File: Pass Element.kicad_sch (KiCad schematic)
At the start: 7 parts, among them Q601 BC846, Q602 MCU18P10Y-TP

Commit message: fix: bom improvements & more notes
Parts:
- D601: Notes (none) -> VZ = 10 V, suitable for input over-voltage clamping
- Q601: Notes (none) -> VCEO > 65 V for 50 V rail, IC small, used as gate pull-down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
- Q602: Notes (none) -> VDS > 100 V, ID > 2 A, P-channel device suitable for high-s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
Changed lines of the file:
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@@
+			)
+		)
+		(property "Notes" "VCEO > 65 V for 50 V rail, IC small, used as gate pull-down switch"
+			(at 149.86 105.41 0)
+			(effects
+				(font
+					(size 1.27 1.27)
+				)
+				(hide yes)
 			)
 		)
@@
 			)
 		)
+		(property "Notes" "VDS > 100 V, ID > 2 A, P-channel device suitable for high-side switching"
+			(at 152.4 64.77 0)
+			(effects
+				(font
+					(size 1.27 1.27)
+				)
+				(hide yes)
+			)
+		)
 		(pin "1"
 		)
@@
 			(at 144.78 78.74 0)
 			(effects
+				(font
+					(size 1.27 1.27)
+				)
+				(hide yes)
+			)
+		)
+		(property "Notes" "VZ = 10 V, suitable for input over-voltage clamping"
+			(at 144.78 78.74 0)
+			(effects

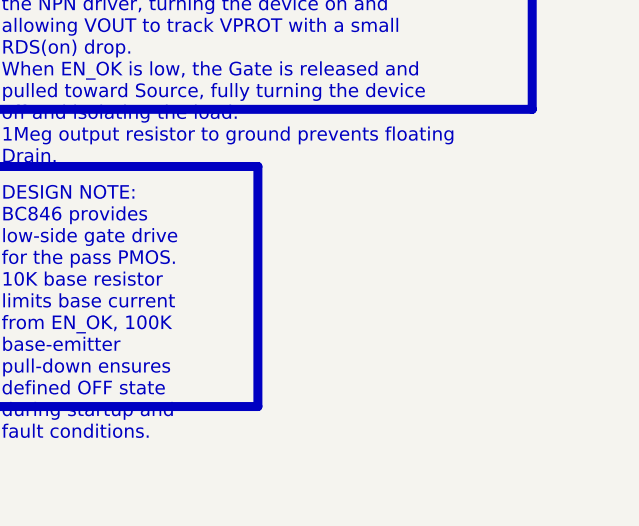
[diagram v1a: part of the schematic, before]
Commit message: feat: ERC/DRC checks
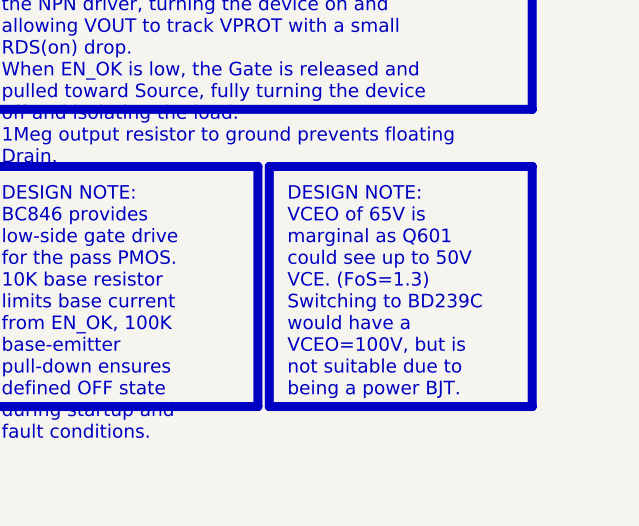
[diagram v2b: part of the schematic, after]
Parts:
- R601, R602, R603, R604: Manufacturer (none) -> Analog Technologies

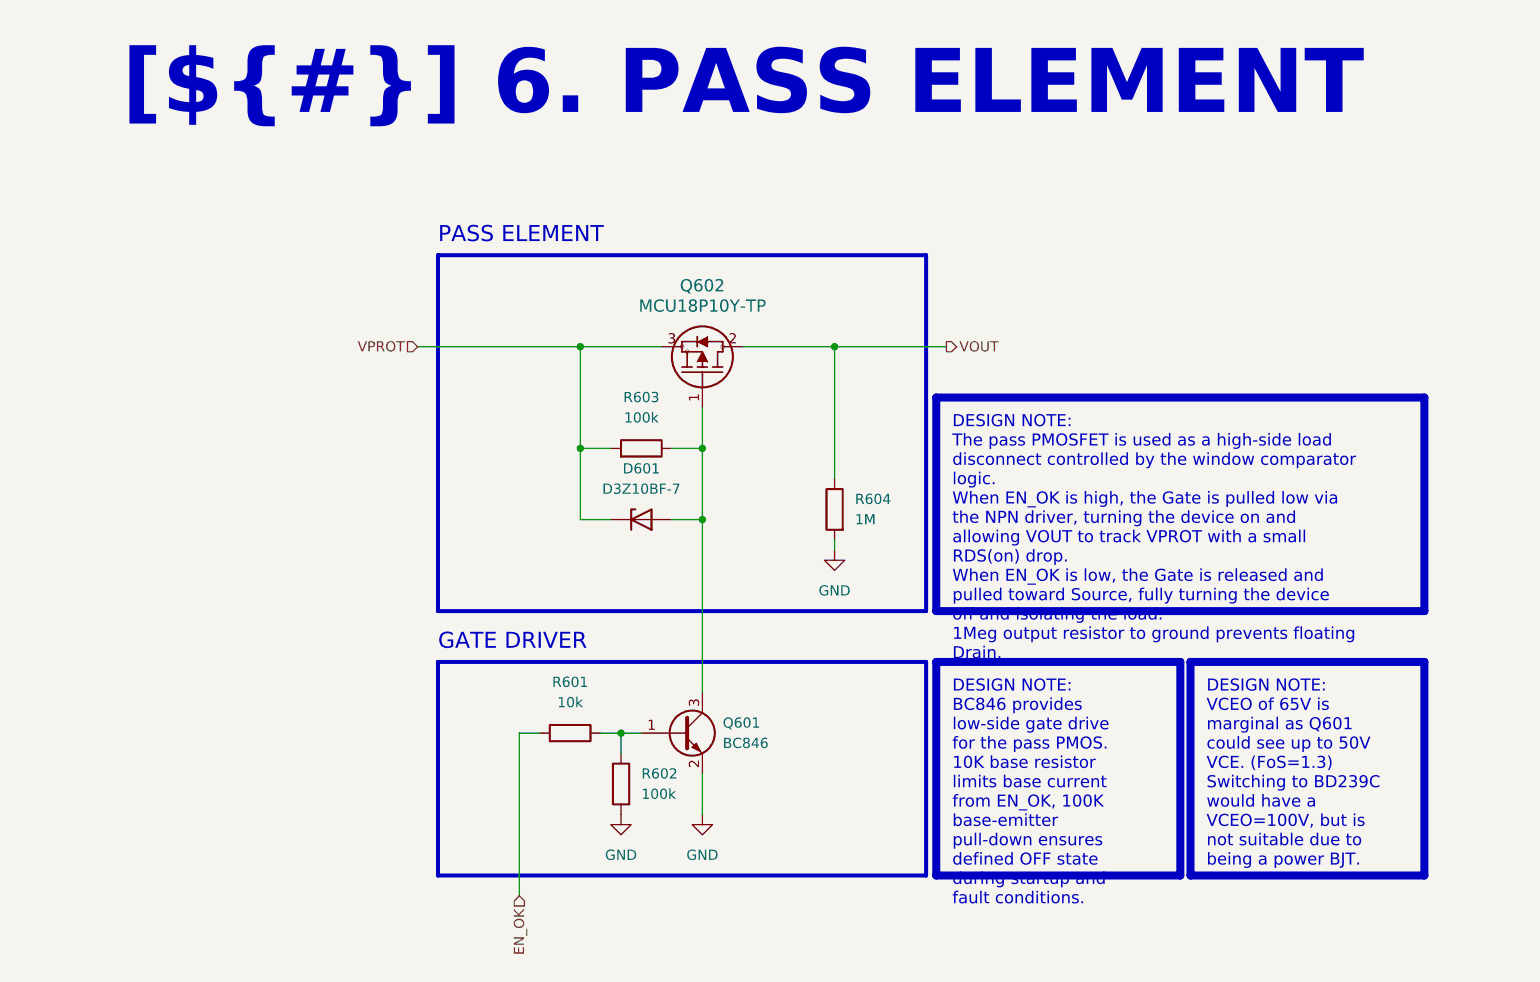
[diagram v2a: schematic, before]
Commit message: feat!: added OC protection, redesigned board from near scratch, size increase
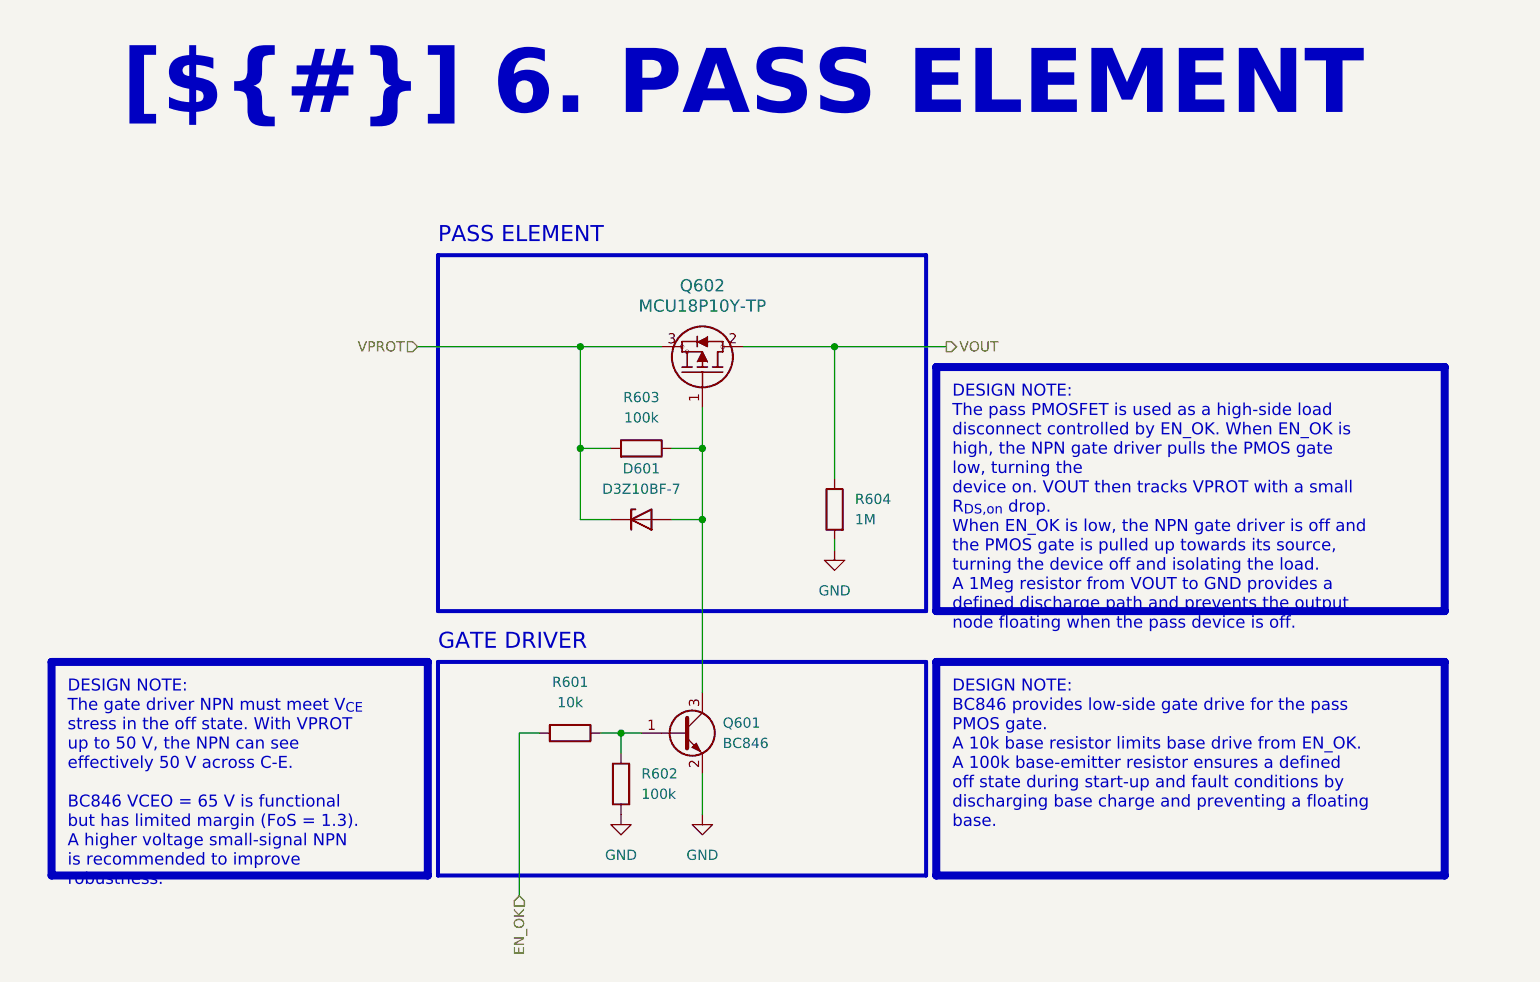
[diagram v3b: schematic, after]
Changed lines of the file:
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@@
 		)
 	)
-	(text_box "DESIGN NOTE:\nThe pass PMOSFET is used as a high-side load disconnect controlled by the window comparator logic. \nWhen EN_OK is high, the Gate is pulled low via the NPN driver, turning the device on and allowing VOUT to track VPROT with a small RDS(on) drop. \nWhen EN_OK is low, the Gate is released and pulled toward Source, fully turning the device off and isolating the load.\n1Meg output resistor to ground prevents floating Drain."
+	(text_box "DESIGN NOTE:\nThe pass PMOSFET is used as a high-side load disconnect controlled by EN_OK. When EN_OK is high, the NPN gate driver pulls the PMOS gate low, turning the\ndevice on. VOUT then tracks VPROT with a small R_{DS,on} drop.\nWhen EN_OK is low, the NPN gate driver is off and the PMOS gate is pulled up towards its source, turning the device off and isolating the load.\nA 1Meg resistor from VOUT to GND provides a defined discharge path and prevents the output node floating when the pass device is off."
 		(exclude_from_sim no)
-		(at 181.61 63.5 0)
-		(size 60.96 26.67)
+		(at 181.61 59.69 0)
+		(size 63.5 30.48)
 		(margins 2 2 2 2)
 		(stroke
@@
 		)
 	)
-	(text_box "DESIGN NOTE:\nVCEO of 65V is marginal as Q601 could see up to 50V VCE. (FoS=1.3)\nSwitching to BD239C would have a VCEO=100V, but is not suitable due to being a power BJT."
+	(text_box "DESIGN NOTE:\nThe gate driver NPN must meet V_{CE} stress in the off state. With VPROT up to 50 V, the NPN can see effectively 50 V across C-E.\n\nBC846 VCEO = 65 V is functional but has limited margin (FoS = 1.3). A higher voltage small-signal NPN is recommended to improve robustness."
 		(exclude_from_sim no)
-		(at 213.36 96.52 0)
-		(size 29.21 26.67)
+		(at 71.12 96.52 0)
+		(size 46.99 26.67)
 		(margins 2 2 2 2)
 		(stroke
@@
 		)
 	)
-	(text_box "DESIGN NOTE:\nBC846 provides low-side gate drive for the pass PMOS. 10K base resistor limits base current from EN_OK, 100K base-emitter pull-down ensures defined OFF state during startup and fault conditions."
+	(text_box "DESIGN NOTE:\nBC846 provides low-side gate drive for the pass PMOS gate.\nA 10k base resistor limits base drive from EN_OK. A 100k base-emitter resistor ensures a defined off state during start-up and fault conditions by discharging base charge and preventing a floating base."
 		(exclude_from_sim no)
 		(at 181.61 96.52 0)
-		(size 30.48 26.67)
+		(size 63.5 26.67)
 		(margins 2 2 2 2)
 		(stroke
